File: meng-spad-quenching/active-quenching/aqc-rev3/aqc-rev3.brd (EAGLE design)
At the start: 120 x 74.9 mm, 299 parts, among them IC1 TPS7A4901, IC10 TPS7A3001, IC11 LT1534-1, IC12 74AHC1G04DBV, IC13 74AHC1G04DBV, IC14 NC7WZ16P6X, IC15 LTC1711, IC16 TLV272DGK, IC17 TLV271DBV, IC18 USBLC6-2SC6Y, IC19 ALD1107, IC2 TPS7A4901, IC20 ALD1106, IC21 STM32F411RE, IC22 MAX572X, IC23 TLV271DBV, IC24 LM1117, IC3 LT1534-1, IC4 74AHC1G04DBV, IC5 ADCMP582, IC6 DS1100LU-20+, IC7 74AHC1G04DBV, IC8 NC7SV74K8X, IC9 TLV272DGK, M1 BSS806N, M2 BSS806N, M3 BSS806N, Q1 MMBTH81, Q2 MMBTH81, Q3 MMBTH81, Q4 MMBTH81, Q5 MMBTH81, Q6 IRLML6402TRPBF, SW1 MCU_RST, T1 MMBTH10, T2 MMBTH10, T3 MMBTH10, T4 MMBTH10, T5 MMBTH10, T6 MMBTH10, T7 MMBTH10, U1 MCP4725, U2 SN65EPT22DGK, U3 SN65EPT21DGK, X1 CONN_PULLDN_SENSE, X2 CONN_FORCE_QUENCH, X3 KEYSTONE-7774, X4 CONN_SPAD, X5 CONN_PHOTON_COUNTER, X6 KEYSTONE-7774, X7 CONN_SMU, X8 PN61729-S

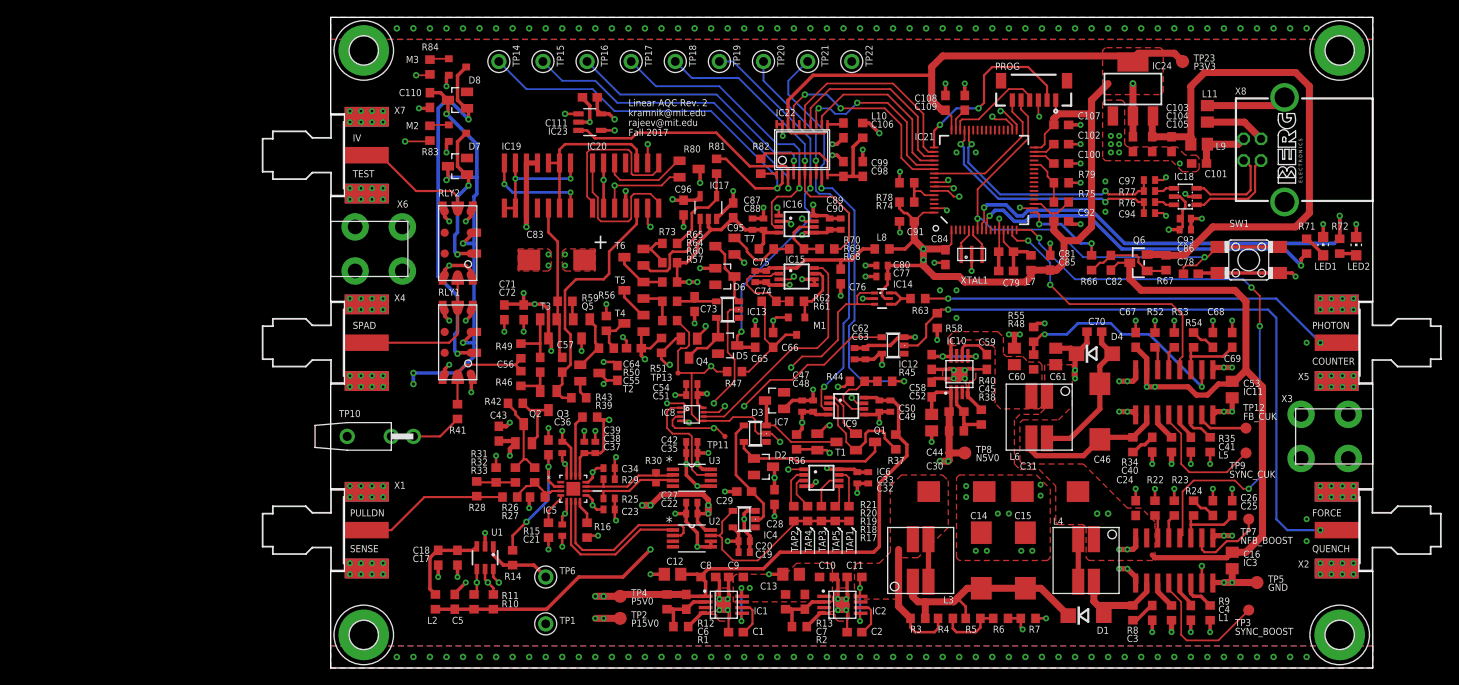
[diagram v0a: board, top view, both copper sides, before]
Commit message: Started plant raman, aqc-rev3, and sense1 wirebonder
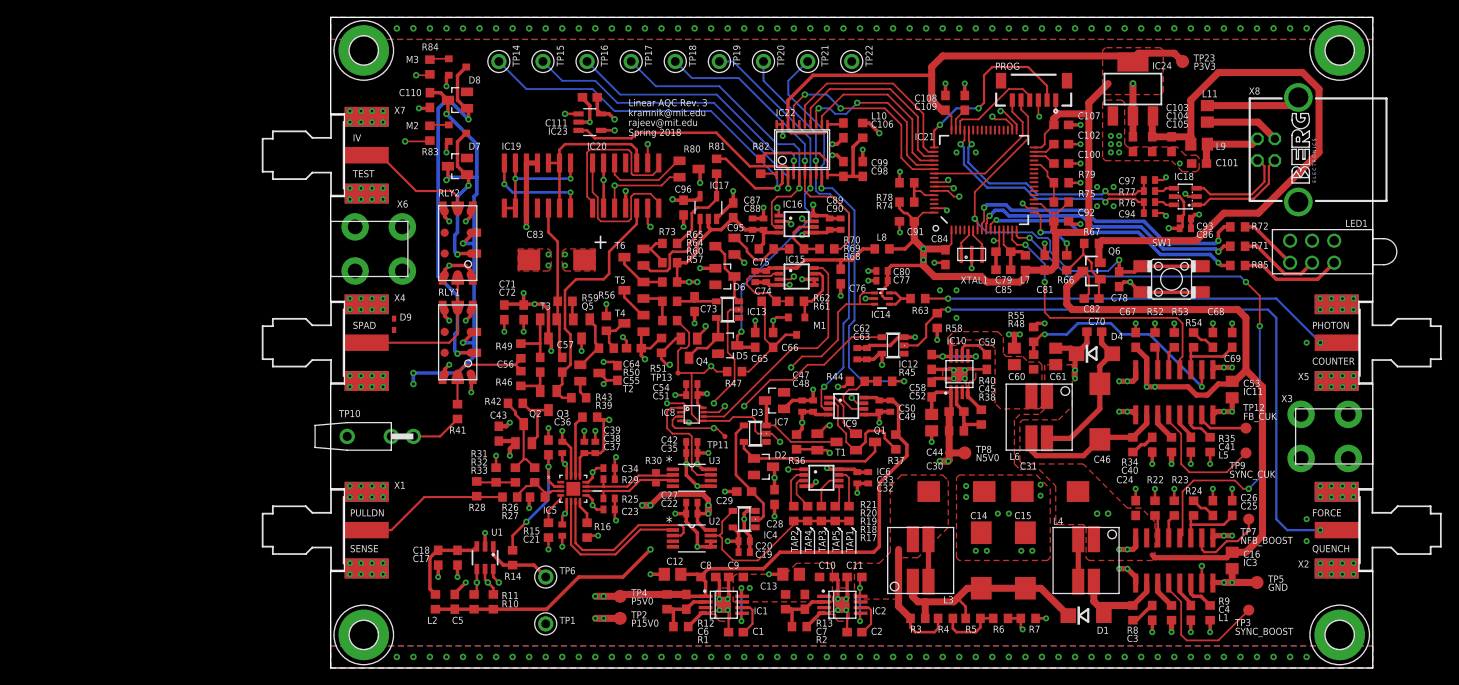
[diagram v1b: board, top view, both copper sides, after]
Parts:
- removed LED2: (no value), led:CHIP-LED0805
- added D9: (no value), diode:SOD523
- added R85: 470R, resistor:R0603
- LED1: value (none) -> 5640200132F; device led:CHIP-LED0805 -> meng:CBI-564-0X00-XXX
- moved R72 12.0 mm to (104.5, 50.8), turned to 180 degrees
- moved SW1 9.16 mm to (96.8, 44.8)
- moved R67 8.86 mm to (87.6, 48.9), turned to 0 degrees
- moved C78 8.28 mm to (90.8, 44.8), turned to 270 degrees
- moved R71 7.94 mm to (104.5, 48.6), turned to 180 degrees
- moved Q6 5.48 mm to (87.6, 45.7)
- moved C82 4.69 mm to (87.6, 42.5), turned to 180 degrees
- moved R66 2.86 mm to (84.8, 46.7)
- moved X8 1.59 mm to (111.4, 59.7)
- moved LED1 1.42 mm to (113.0, 47.9), turned to 90 degrees
- moved C81 0.64 mm to (82.2, 46.7)
- moved C80 0.63 mm to (63.5, 45.7)
- moved L7 0.63 mm to (80.0, 46.7)
- moved C77 0.48 mm to (63.5, 44.6)
- moved C79 0.35 mm to (77.5, 45.9)
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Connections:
- new net MCU_LED3: IC21.10, R85.2
- new net N$31: LED1.BOT_A, R85.1
- net GND: now also D9.A, LED1.BOT_K, LED1.MID_K, LED1.TOP_K; no longer LED1.C, LED2.C
- net N$24: now also LED1.MID_A; no longer LED1.A
- net N$9: now also LED1.TOP_A; no longer LED2.A
- net V_SPAD: now also D9.C
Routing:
- net MCU_LED3: track 0.00 -> 30.6 mm, vias 0 -> 2
- net MCU_LED1: track 51.6 -> 34.4 mm
- net N$31: track 0.00 -> 11.7 mm
- net MCU_LED2: track 42.7 -> 32.0 mm
- net SMPS_USB_VDD: track 253.6 -> 262.5 mm
- net MCU_NRST: track 58.5 -> 49.8 mm
- net GND: track 333.7 -> 326.6 mm
- net N$24: track 3.03 -> 9.56 mm
- net N$9: track 1.99 -> 6.89 mm
- net USB_VDD: track 63.9 -> 68.1 mm
- net !MCU_SMPS_PRECHG: track 10.1 -> 7.73 mm
- net PP_P3V3: track 368.9 -> 367.2 mm
- net USBCONN_P4: track 6.98 -> 8.57 mm
- net USBCONN_P1: track 6.70 -> 8.29 mm
- net !MCU_SHDN_CUK: track 32.0 -> 33.5 mm
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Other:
- board text added: "Linear AQC Rev. 3 kramnik@mit.edu rajeev@mit.edu Spring 2018"
- board text added: "Linear Active SPAD Quenching Circuit Rev. 3 kramnik@mit.edu rajeev@mit.edu Spring 2018"
- board text removed: "Linear AQC Rev. 2 kramnik@mit.edu rajeev@mit.edu Fall 2017"
- board text removed: "Linear Active SPAD Quenching Circuit Rev. 2 kramnik@mit.edu rajeev@mit.edu Fall 2017"

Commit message: Work on new leaf heater and AQC with new BJTs, level shift topology
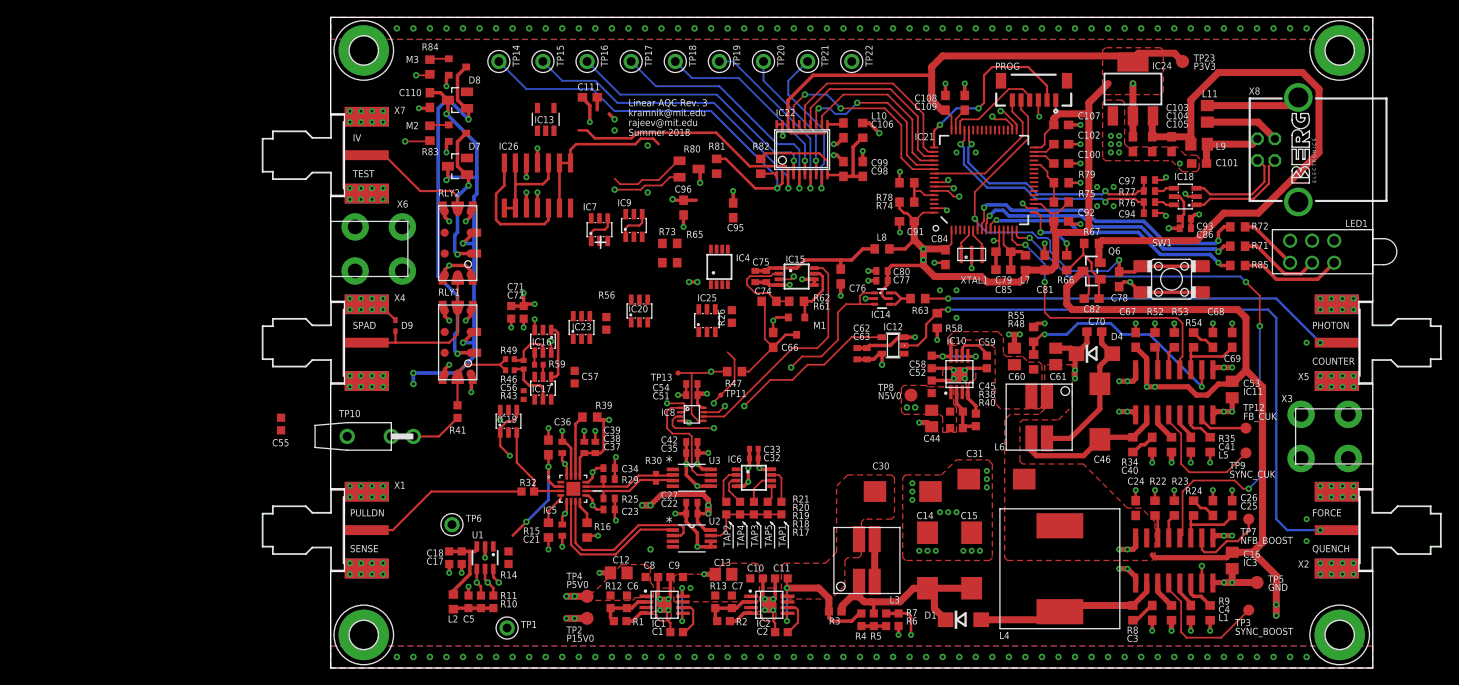
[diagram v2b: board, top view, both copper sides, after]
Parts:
- removed C19, C48, C50, C87, C89: 100n, rcl:C0402
- removed C20, C47, C49, C88, C90: 10n, rcl:C0402
- removed C28, C65: 470p, rcl:C0603
- removed C29, C73: 10p, rcl:C0603
- removed C43, C64: 100n, rcl:C0603
- removed C83: 47u, 20V, rcl:CT7343
- removed D2, D3, D5, D6: BAS40, diode:SOT23
- removed Q1, Q2, Q3, Q4, Q5: MMBTH81, transistor-pnp:SOT23-BEC
- removed R27, R31, R42, R57: DNP, rcl:R0603
- removed R28, R33, R60: 0R, rcl:R0603
- removed R36, R37, R51, R64, R68: 470R, rcl:R0603
- removed R44, R45, R69, R70: 100k, rcl:R0603
- removed R50: 49R9, rcl:R0603
- removed T1, T2, T3, T4, T5, T6, T7: MMBTH10, transistor:SOT23-BEC
- added IC25: HFA3134, meng:SOT23-6L
- added IC26: THAT320, meng:SO14
- C1, C10, C11, C17, C18, C2, C45, C5, C52, C55, C57, C58, C59, C6, C7, C71, C72, C8, C9: device rcl:C0603 -> rcl-modified-footprints:C0603
- C32, C33: device rcl:C0402 -> rcl-modified-footprints:C0402
- C56: value 10n -> 100p; device rcl:C0603 -> rcl-modified-footprints:C0402
- IC13: value 74AHC1G04DBV -> TLV271DBV; device 74xx-little-de:SOT23-5 -> meng:SOT23-5
- IC16, IC9: value TLV272DGK -> HFA3134; device meng:MSOP8 -> meng:SOT23-6L
- IC17: value TLV271DBV -> HFA3135; device meng:SOT23-5 -> meng:SOT23-6L
- IC19: value ALD1107 -> HFA3135; device meng:SO14 -> meng:SOT23-6L
- IC20: value ALD1106 -> HFA3134; device meng:SO14 -> meng:SOT23-6L
- IC23: value TLV271DBV -> HFA3134; device meng:SOT23-5 -> meng:SOT23-6L
- IC4: value 74AHC1G04DBV -> TLV272DGK; device 74xx-little-de:SOT23-5 -> meng:MSOP8
- IC7: value 74AHC1G04DBV -> HFA3134; device 74xx-little-de:SOT23-5 -> meng:SOT23-6L
- L4: value SRF0703-820M -> 732-1699-2-ND; device meng:SRF0703 -> meng:WE_INDUCTOR_SIZE_CODE_1210
- R1, R12, R13, R2, R3, R38, R4, R40, R5, R6, R7: device resistor:R0603 -> rcl-modified-footprints:R0603
- R10, R11, R14, R17, R18, R19, R20, R21, R41, R56: device rcl:R0603 -> rcl-modified-footprints:R0603
- R26: value DNP -> 220R; device rcl:R0603 -> rcl-modified-footprints:R0603
- R32: value 1k -> 220R; device rcl:R0603 -> rcl-modified-footprints:R0603
- R43, R59: value 200R -> 220R; device rcl:R0603 -> rcl-modified-footprints:R0402
- R46, R49: device rcl:R0603 -> rcl-modified-footprints:R0402
- TP20: value DELAY_UP -> (DELAY_UP)
- TP21: value DELAY_DN -> (DELAY_DN)
- X1, X2, X4, X5, X7: device meng:J502-ND-142-0711-871/876 -> meng:J502-ND-142-0701-881/886
- moved C55 39.2 mm to (-5.71, 28.1), turned to 270 degrees
- moved R26 33.0 mm to (46.2, 40.5), turned to 90 degrees
- moved IC16 32.2 mm to (24.4, 37.6), turned to 180 degrees
- moved IC9 32.1 mm to (34.9, 51.0), turned to 0 degrees
- moved IC13 30.3 mm to (24.8, 63.2), turned to 0 degrees
- moved IC7 29.6 mm to (31.0, 50.5), turned to 0 degrees
- moved IC4 29.2 mm to (44.8, 46.2), turned to 0 degrees
- moved IC17 28.2 mm to (24.4, 32.2), turned to 180 degrees
- moved IC19 27.4 mm to (20.5, 28.4)
- moved IC23 23.7 mm to (28.9, 39.2), turned to 0 degrees
- moved R7 14.9 mm to (65.4, 5.56), turned to 270 degrees
- moved IC20 14.5 mm to (35.6, 41.1)
- moved D1 14.1 mm to (72.9, 5.56)
- moved C33 13.6 mm to (48.7, 25.2), turned to 180 degrees
- moved R6 13.2 mm to (64.0, 5.56), turned to 270 degrees
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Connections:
- net VREF_CASCODE_IBIAS renamed VREF_DELTAV_SETPOINT
- removed net CASC_BIAS_B: IC17.1, T6.B
- removed net CASC_BIAS_C: R64.2, T5.E, T6.C
- removed net CASC_BIAS_E: R65.2, R73.1, T6.E
- removed net CASC_BIAS_VGND: IC17.4, R73.2, R81.1
- removed net CASC_MIDPT: T4.E, T5.C
- removed net DELAY_CAP: C29.1, IC4.2, IC7.4
- removed net DIAMOND_IBIAS_NMOS: C57.2, IC20.5, Q3.B, R43.1
- removed net DIAMOND_IBIAS_PMOS: C57.1, IC19.5, R59.2, T3.B
- removed net LBOOST_!: L4.2, L4.3
- removed net N$1: IC16.2, Q4.E, R51.1
- removed net N$17: D6.3, IC13.3, T7.C
- removed net N$2: R57.1, R60.1, T5.B
- removed net N$21: Q5.B, R50.1, T2.B
- removed net N$22: R50.2, R56.1, T4.C
- removed net N$27: Q2.C, R32.2, R33.2, R42.1
- removed net N$32: R26.1, R28.1, X1.1
- removed net N$38: IC16.1, Q4.B
- removed net N$42: IC16.7, T7.B
- removed net N$43: IC16.6, R69.2, R70.1
- removed net N$44: D2.1, IC7.5, Q1.C
- removed net N$45: D3.3, IC7.3, T1.C
- removed net N$46: IC9.7, T1.B
- removed net N$47: IC9.6, R44.2, R45.1
- removed net N$48: IC9.2, Q1.E, R37.1
- removed net N$49: IC9.1, Q1.B
- removed net N$50: IC20.3, IC23.4, R80.2
- removed net N$7: D5.1, IC13.5, Q4.C
- removed net N$78: IC20.13, IC20.2, IC23.1
- removed net N$81: IC20.12, R80.1
- removed net N$82: R68.2, R69.1, T7.E
- removed net N$86: R36.2, R44.1, T1.E
- removed net N$90: IC19.10, IC19.6, IC19.9, IC20.10
- removed net NC_IC15_V+: IC20.11
- removed net NC_IC16_V-: IC19.4
- removed net QUENCH_WFM: C73.1, IC13.4, R60.2
- removed net VREF_DELAY_DN: IC22.9, R45.2, TP21.P$1
- removed net VREF_DELAY_UP: IC22.8, IC9.3, TP20.P$1
- removed net VREF_SLEW_DN: IC22.6, R70.2, TP18.P$1
- removed net VREF_SLEW_MAX: C65.1, D5.3, IC22.7, TP19.P$1
- removed net VREF_SLEW_UP: IC16.3, IC22.5, TP17.P$1
- new net CCS_STEERING_TAIL: IC20.2, IC20.5, IC25.6
- new net CCS_VA_SETPOINT: IC23.5, IC25.3
- new net DELTAV_BASE: IC25.1, IC4.1
- new net DELTAV_FB: IC25.2, R65.2, R73.1
- new net DELTAV_VGND: IC4.2, R73.2, R81.1
- new net DIAMOND_BASE: IC13.1, IC7.1, IC7.4
- new net DIAMOND_FB: IC13.4, IC7.2, R80.2
- new net DIAMOND_FB_R: IC7.5, R80.1
- new net DIAMOND_IBIAS_BOTTOM: C57.2, IC17.4, IC9.3, R43.1
- new net DIAMOND_IBIAS_MID: IC26.6, IC26.8, IC26.9, IC9.6
- new net DIAMOND_IBIAS_TOP: C57.1, IC16.4, IC26.7, R59.2
- new net DIAMOND_IN: IC16.1, IC17.1, IC23.3, IC23.6, R56.1
- new net N$30: IC17.6, IC19.2
- new net N$35: IC20.3, IC23.2
- new net VA_BASE: IC25.4, IC4.7
- new net VA_FB: IC25.5, IC4.6, R26.2
- new net VREF_EXTRA_1: IC22.6, TP18.P$1
- new net VREF_EXTRA_2: IC22.7, TP19.P$1
- new net VREF_EXTRA_3: IC22.8, TP20.P$1
- new net VREF_EXTRA_4: IC22.9, TP21.P$1
- new net VREF_VA_SETPOINT: IC22.5, IC4.5, TP17.P$1
- net !LOGIC_QUENCH: now also IC20.1; no longer IC13.2
- net BLANKING_LATCH_EN: no longer IC4.4
- net BOOST_SW_NODE: now also L4.2; no longer L4.4
- net GND: now also IC13.2, IC19.6, IC26.11, IC26.4, R26.1; no longer C19.2, C20.2, C28.2, C29.2, C43.2, C47.2, C48.2, C49.2, C50.2, C64.2, C65.2, C73.2, C83.-, C87.2, C88.2, C89.2, C90.2, D3.1, D6.1, IC16.5, IC17.3, IC20.4, IC23.2, IC9.5, Q5.C, R27.1, R31.1
- net LOGIC_QUENCH: now also IC20.4; no longer IC7.2, R57.2
- net N$10: now also IC17.3, IC19.5; no longer Q2.E, Q3.C, R42.2
- net N$11: now also IC17.2; no longer Q5.E
- net N$13: now also IC16.2; no longer T2.E
- net N$14: now also IC17.5; no longer Q3.E
- net N$16: now also IC7.6, IC9.2; no longer IC20.1, IC20.8
- net N$26: now also IC7.3, IC9.5; no longer IC20.14, IC20.7
- net N$28: now also X1.1; no longer R28.2, R31.2
- net N$5: now also IC16.5; no longer T3.E
- net N$88: now also IC26.1, IC26.10, IC26.13, IC26.2; no longer IC19.1, IC19.13, IC19.2, IC19.8
- net N$89: now also IC26.14, IC26.5; no longer IC19.14, IC19.7
- net PP_N5V0_ANALOG: now also IC4.4; no longer C47.1, C48.1, C87.1, C88.1, IC16.4, IC17.2, IC9.4, R36.1, R64.1, R68.1
- net PP_P15V0_ANALOG: now also IC16.3, IC16.6, IC26.12, IC26.3; no longer C83.+, IC19.11, IC19.12, IC19.3, T2.C, T3.C
- net PP_P3V3: no longer C19.1, C20.1, C28.1, D2.3, IC4.5
- net PP_P5V0_ANALOG: now also IC13.5, IC19.1, IC19.4, IC23.1, IC23.4, IC4.8, IC9.1, IC9.4; no longer C43.1, C49.1, C50.1, C64.1, C89.1, C90.1, IC16.8, IC17.5, IC20.9, IC23.5, IC9.8, Q2.B, R37.2, R51.2, T4.B
- net SPAD_PULLDN_SENSE: now also IC19.3, R32.2; no longer R26.2, R27.2, R33.1
- net VREF_DIAMOND_IBIAS: now also IC13.3; no longer IC23.3
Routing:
- net PP_P5V0_ANALOG: track 220.3 -> 129.0 mm, vias 12 -> 10
- net PP_P3V3: track 367.2 -> 287.3 mm, vias 19 -> 17
- net PP_N5V0_ANALOG: track 154.9 -> 90.2 mm, vias 6 -> 5
- net VREF_DELAY_DN: track 50.5 -> 0.00 mm, vias 2 -> 0
- net VREF_DELAY_UP: track 48.4 -> 0.00 mm, vias 2 -> 0
- net VREF_SLEW_MAX: track 45.7 -> 0.00 mm, vias 2 -> 0
- net GND: track 326.6 -> 287.9 mm, vias 366 -> 355
- net VREF_SLEW_UP: track 36.9 -> 0.00 mm, vias 1 -> 0
- net VREF_SLEW_DN: track 35.7 -> 0.00 mm, vias 1 -> 0
- net VREF_VA_SETPOINT: track 0.00 -> 29.6 mm, vias 0 -> 1
- net DIAMOND_IBIAS_NMOS: track 29.4 -> 0.00 mm
- net N$1: track 29.1 -> 0.00 mm, vias 2 -> 0
- net SMPS_USB_VDD: track 262.5 -> 288.5 mm
- net LOGIC_QUENCH: track 63.4 -> 38.9 mm, vias 4 -> 2
- net VREF_EXTRA_1: track 0.00 -> 22.4 mm, vias 0 -> 1
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- added copper zone on layer 1, net PP_N5V0_ANALOG
- added copper zone on layer 1, net PP_P5V0_ANALOG
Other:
- board text added: "Linear AQC Rev. 3 kramnik@mit.edu rajeev@mit.edu Summer 2018"
- board text added: "Linear Active SPAD Quenching Circuit Rev. 3 kramnik@mit.edu rajeev@mit.edu Summer 2018"
- board text removed: "Linear AQC Rev. 3 kramnik@mit.edu rajeev@mit.edu Spring 2018"
- board text removed: "Linear Active SPAD Quenching Circuit Rev. 3 kramnik@mit.edu rajeev@mit.edu Spring 2018"

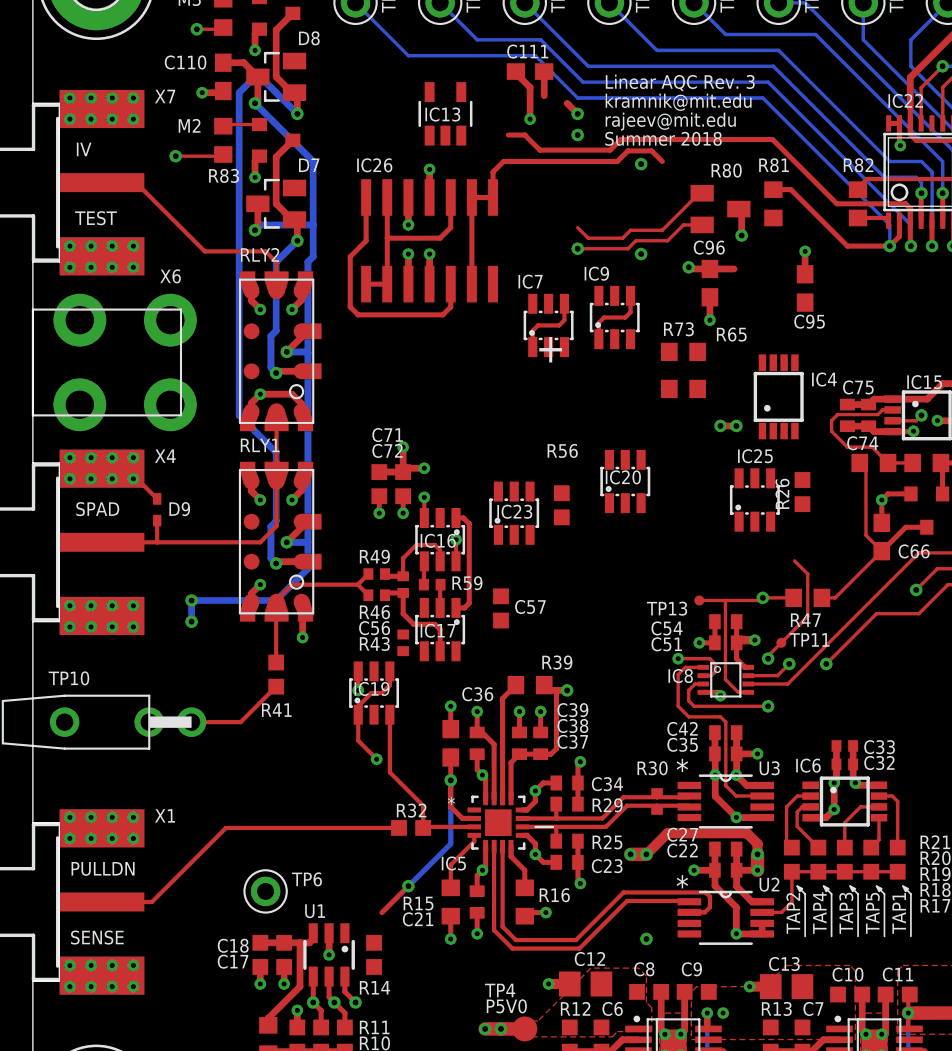
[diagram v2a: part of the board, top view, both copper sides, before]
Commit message: layout work, placed and routed diamond buffer
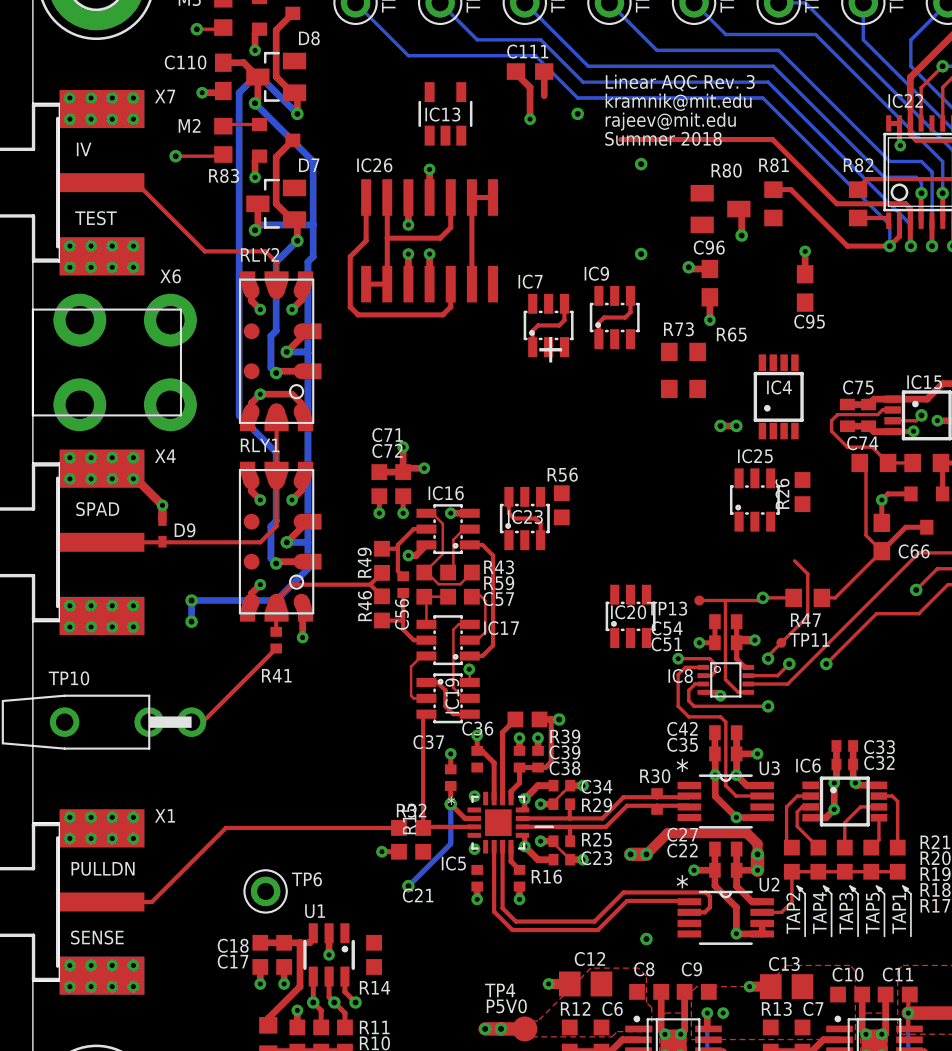
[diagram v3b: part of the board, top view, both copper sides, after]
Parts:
- C21, C23, C34, C37, C38, C39: device rcl:C0402 -> rcl-modified-footprints:C0402
- C36: device rcl:C0603 -> rcl-modified-footprints:C0402
- R15, R39: device rcl:R0603 -> rcl-modified-footprints:R0603
- R16: device rcl:R0603 -> rcl-modified-footprints:R0402
- R25, R29, R30: device rcl:R0402 -> rcl-modified-footprints:R0402
- R41: device rcl-modified-footprints:R0603 -> rcl-modified-footprints:R0402
- R43, R46, R49, R59: device rcl-modified-footprints:R0402 -> rcl-modified-footprints:R0603
- moved IC20 8.10 mm to (35.9, 33.0)
- moved C57 4.82 mm to (23.5, 34.9)
- moved IC19 4.46 mm to (24.9, 28.1), turned to 270 degrees
- moved R43 4.41 mm to (24.9, 34.9)
- moved R15 3.84 mm to (22.7, 18.9), turned to 0 degrees
- moved R59 2.38 mm to (26.4, 34.9), turned to 90 degrees
- moved R39 2.07 mm to (29.7, 26.8)
- moved C36 2.06 mm to (25.1, 23.3)
- moved R41 2.06 mm to (14.6, 31.6)
- moved R16 1.46 mm to (29.2, 17.3)
- moved C21 1.43 mm to (26.7, 17.3)
- moved D9 1.31 mm to (7.78, 38.1)
- moved C39 0.97 mm to (30.3, 24.4)
- moved C37 0.95 mm to (26.7, 24.4)
- moved C38 0.95 mm to (29.2, 24.4)
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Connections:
- net N$10 renamed DMD_OP_CASC
- net N$11 renamed DMD_IN_PNP_E
- net N$13 renamed DMD_IN_NPN_E
- net N$14 renamed DMD_OP_PNP
- net N$23 renamed DMD_OUT
- net N$30 renamed DMD_IN_CASC
- net N$35 renamed STEERING_CASC
- net N$5 renamed DMD_OP_NPN
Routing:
- net PP_P5V0_ANALOG: track 129.0 -> 112.8 mm, vias 10 -> 9
- net DIAMOND_FB: track 15.1 -> 0.18 mm, vias 2 -> 0
- net DIAMOND_IBIAS_MID: track 18.9 -> 6.47 mm
- net DIAMOND_FB_R: track 8.85 -> 0.17 mm
- net PP_P3V3: track 287.3 -> 279.1 mm
- net VREF_DIAMOND_IBIAS: track 63.8 -> 56.4 mm
- net DIAMOND_IBIAS_TOP: track 1.41 -> 8.07 mm
- net DIAMOND_IN: track 6.62 -> 12.9 mm
- net DMD_OP_CASC: track 0.00 -> 5.85 mm
- net COMP_VP: track 14.3 -> 8.83 mm
- net DMD_IN_CASC: track 0.00 -> 3.92 mm
- net COMP_VTN: track 3.73 -> 0.00 mm
- net DMD_IN_NPN_E: track 0.00 -> 3.35 mm
- net DIAMOND_IBIAS_BOTTOM: track 0.00 -> 3.14 mm
- net GND: track 287.9 -> 285.0 mm, vias 355 -> 358
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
